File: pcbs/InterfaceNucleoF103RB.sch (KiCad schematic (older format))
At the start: 4 parts

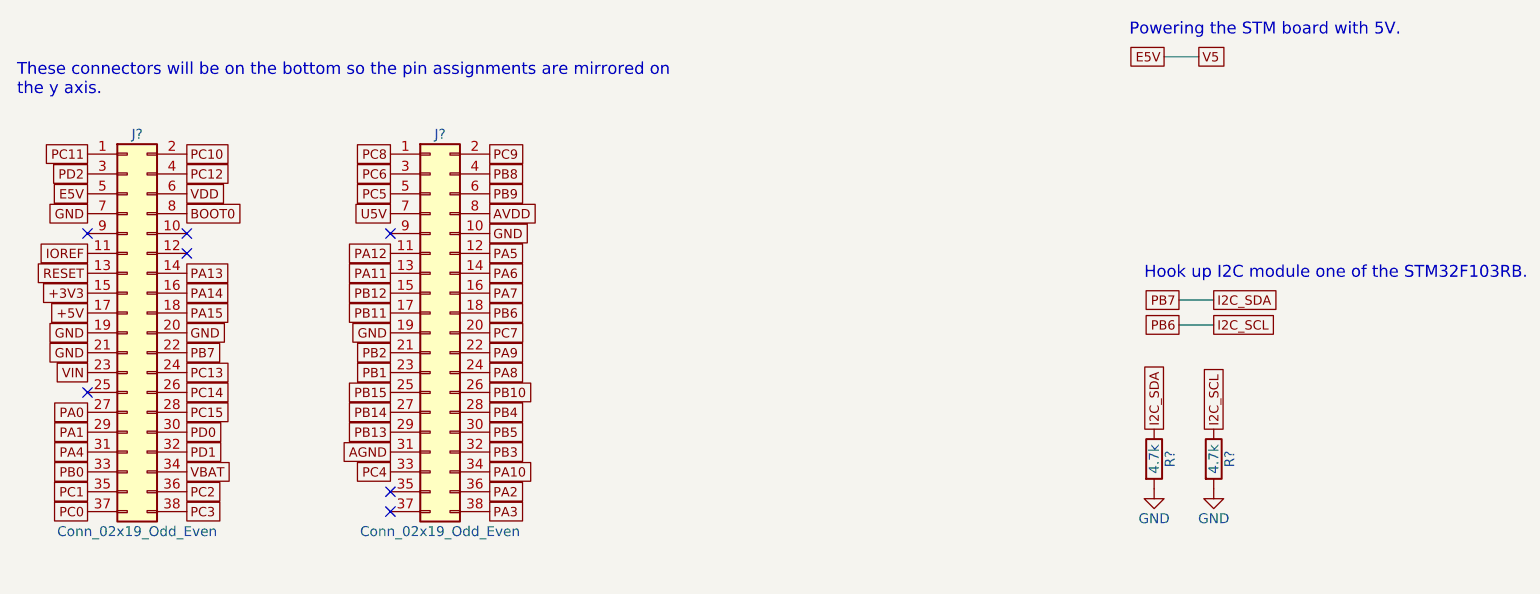
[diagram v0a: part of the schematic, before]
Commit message: Almost done with schematics. SPI OLED is missing.
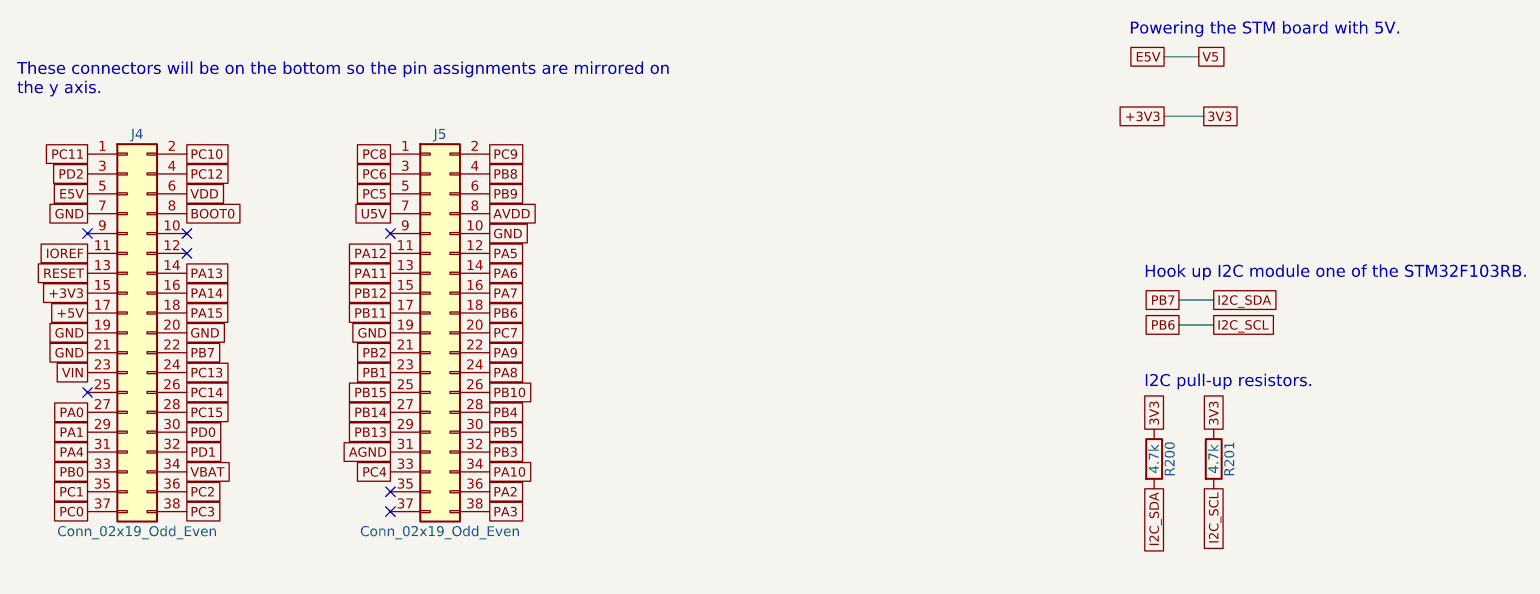
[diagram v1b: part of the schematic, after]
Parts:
- gave numbers to parts that had none: 4
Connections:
- net +3V3: now also R200.1, R201.1
- net GND: no longer R200.2, R201.2
- net I2C_SCL: now also R201.2; no longer R201.1
- net I2C_SDA: now also R200.2; no longer R200.1
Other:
- note added: "I2C pull-up resistors."
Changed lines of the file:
@@
 LIBS:mydacs
 LIBS:mydcdcs
+LIBS:switches
+LIBS:mytactilesw
 LIBS:led_driver-cache
 EELAYER 25 0
@@
 $EndDescr
 $Comp
-L Conn_02x19_Odd_Even J?
+L Conn_02x19_Odd_Even J4
 U 1 1 5A0C4E25
 P 2830 3565
-F 0 "J?" H 2880 4565 50  0000 C CNN
+F 0 "J4" H 2880 4565 50  0000 C CNN
 F 1 "Conn_02x19_Odd_Even" H 2880 2565 50  0000 C CNN
 F 2 "" H 2830 3565 50  0001 C CNN
@@
 NoConn ~ 2630 3865
 $Comp
-L Conn_02x19_Odd_Even J?
+L Conn_02x19_Odd_Even J5
 U 1 1 5A0C5DFF
 P 4355 3565
-F 0 "J?" H 4405 4565 50  0000 C CNN
+F 0 "J5" H 4405 4565 50  0000 C CNN
 F 1 "Conn_02x19_Odd_Even" H 4405 2565 50  0000 C CNN
 F 2 "" H 4355 3565 50  0001 C CNN
@@
 Text GLabel 8225 2175 2    47   UnSpc ~ 0
 V5
-Wire Wire Line
-	8050 2175 8225 2175
 Text Notes 7875 2075 0    60   ~ 0
 Powering the STM board with 5V.
@@
 Text GLabel 8300 3400 2    47   UnSpc ~ 0
 I2C_SDA
-Wire Wire Line
-	8125 3400 8300 3400
 Text GLabel 8125 3525 0    47   UnSpc ~ 0
 PB6
 Text GLabel 8300 3525 2    47   UnSpc ~ 0
 I2C_SCL
-Wire Wire Line
-	8125 3525 8300 3525
-$Comp
-L R R?
+$Comp
+L R R200
 U 1 1 5A0C91BF
 P 8000 4200
-F 0 "R?" V 8080 4200 50  0000 C CNN
+F 0 "R200" V 8080 4200 50  0000 C CNN
 F 1 "4.7k" V 8000 4200 50  0000 C CNN
 F 2 "Resistors_SMD:R_0603" V 7930 4200 50  0001 C CNN
@@
 $EndComp
 $Comp
-L R R?
+L R R201
 U 1 1 5A0C92CA
 P 8300 4200
-F 0 "R?" V 8380 4200 50  0000 C CNN
+F 0 "R201" V 8380 4200 50  0000 C CNN
 F 1 "4.7k" V 8300 4200 50  0000 C CNN
 F 2 "Resistors_SMD:R_0603" V 8230 4200 50  0001 C CNN
@@
 	1    0    0    -1
 $EndComp
+Text GLabel 8300 4350 3    47   UnSpc ~ 0
+I2C_SCL
+Text GLabel 8000 4350 3    47   UnSpc ~ 0
+I2C_SDA
+Text GLabel 8050 2475 0    47   UnSpc ~ 0
++3V3
+Text GLabel 8250 2475 2    47   UnSpc ~ 0
+3V3
+Text GLabel 8000 4050 1    47   UnSpc ~ 0
+3V3
 Text GLabel 8300 4050 1    47   UnSpc ~ 0
-I2C_SCL
-Text GLabel 8000 4050 1    47   UnSpc ~ 0
-I2C_SDA
-$Comp
-L GND #PWR?
-U 1 1 5A0C94D9
-P 8000 4350
-F 0 "#PWR?" H 8000 4100 50  0001 C CNN
-F 1 "GND" H 8000 4200 50  0000 C CNN
-F 2 "" H 8000 4350 50  0001 C CNN
-F 3 "" H 8000 4350 50  0001 C CNN
-	1    8000 4350
-	1    0    0    -1
-$EndComp
-$Comp
-L GND #PWR?
-U 1 1 5A0C94F7
-P 8300 4350
-F 0 "#PWR?" H 8300 4100 50  0001 C CNN
-F 1 "GND" H 8300 4200 50  0000 C CNN
-F 2 "" H 8300 4350 50  0001 C CNN
-F 3 "" H 8300 4350 50  0001 C CNN
-	1    8300 4350
-	1    0    0    -1
-$EndComp
+3V3
+Wire Wire Line
+	8050 2175 8225 2175
+Wire Wire Line
+	8125 3400 8300 3400
+Wire Wire Line
+	8125 3525 8300 3525
+Wire Wire Line
+	8050 2475 8250 2475
+Text Notes 7950 3850 0    60   ~ 0
+I2C pull-up resistors.
 $EndSCHEMATC

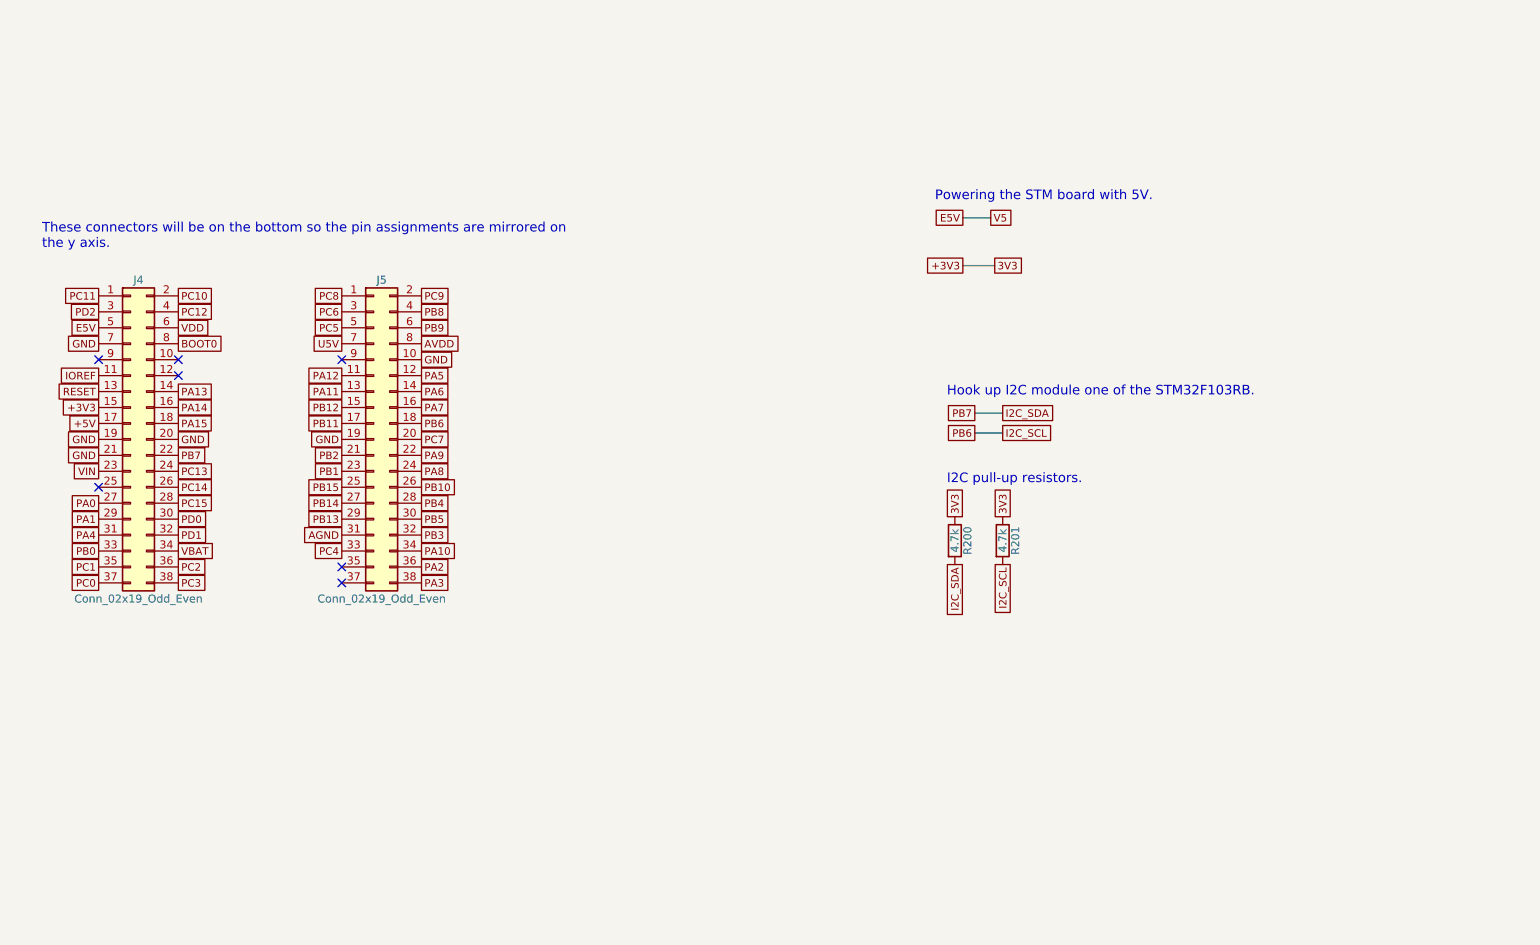
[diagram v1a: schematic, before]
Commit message: No DRC errors anymore in schematics.
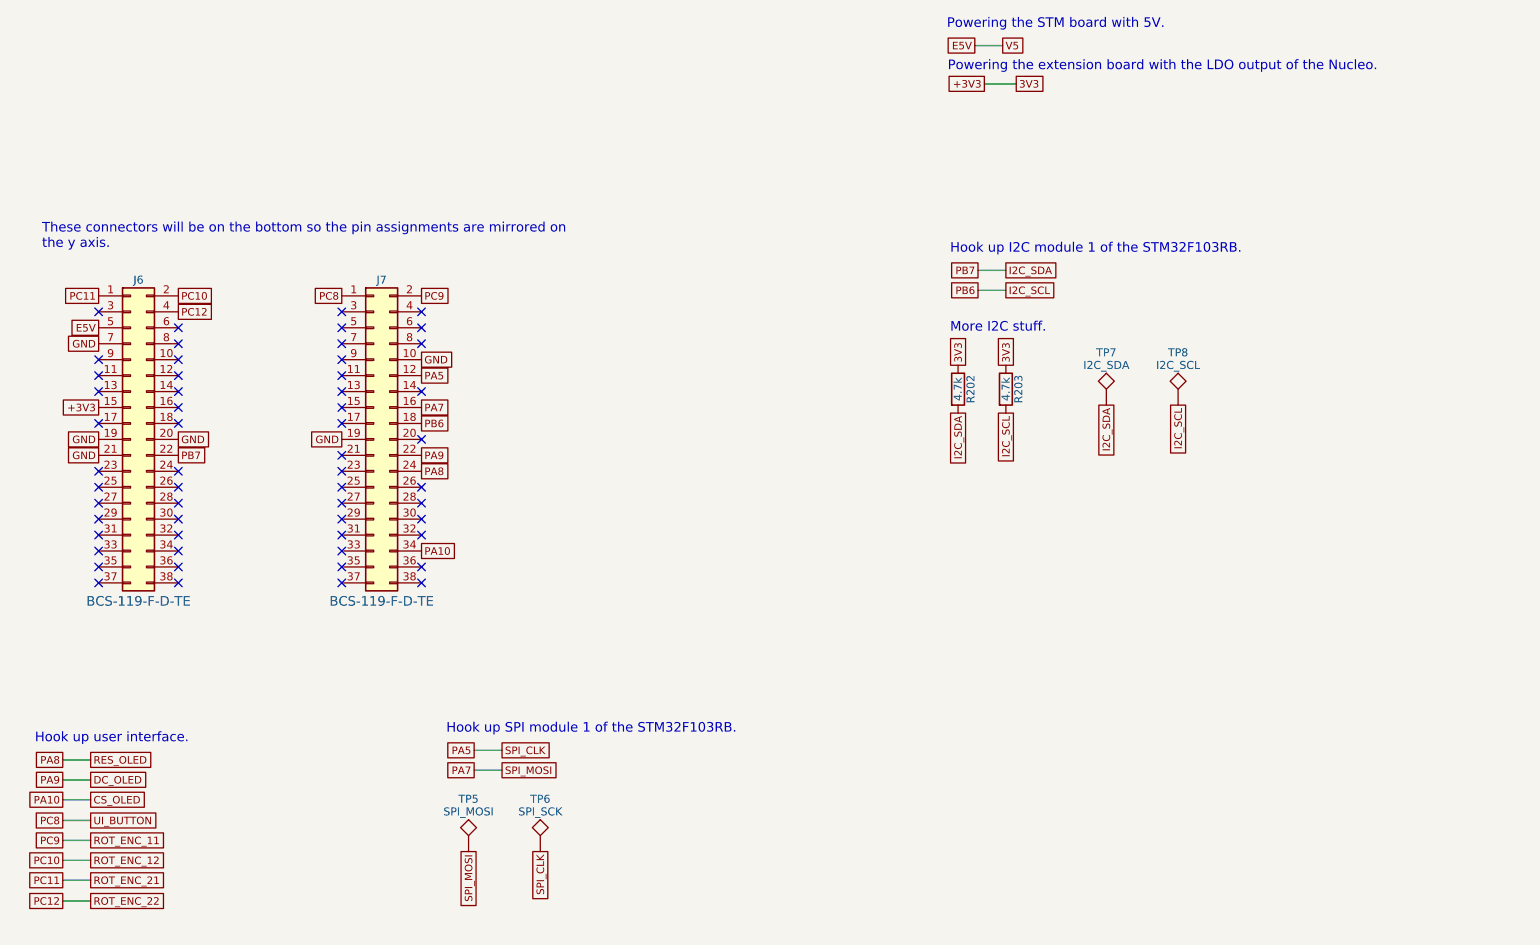
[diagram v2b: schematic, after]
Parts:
- removed J5: Conn_02x19_Odd_Even, symbol Conn_02x19_Odd_Even
- added J7: Conn_02x19_Odd_Even, Pin_Headers:Pin_Header_Straight_2x19_Pitch2.54mm, symbol Conn_02x19_Odd_Even
- added TP5: SPI_MOSI, MyTestpoints:TP_SMD_quadr_1mm, symbol TEST
- added TP6: SPI_SCK, MyTestpoints:TP_SMD_quadr_1mm, symbol TEST
- added TP7: I2C_SDA, MyTestpoints:TP_SMD_quadr_1mm, symbol TEST
- added TP8: I2C_SCL, MyTestpoints:TP_SMD_quadr_1mm, symbol TEST
- J6: renamed from J4; footprint (none) -> Pin_Headers:Pin_Header_Straight_2x19_Pitch2.54mm; Samtec (none) -> BCS-119-F-D-TE
- renumbered R200 to R202, R201 to R203
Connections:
- net GND: now also J7.10 (Pin_10), J7.19 (Pin_19)
- net I2C_SCL: now also J7.18 (Pin_18), TP8.1
- net I2C_SDA: now also TP7.1
- net PA5: now also J7.12 (Pin_12), TP6.1
- net PA7: now also J7.16 (Pin_16), TP5.1
- net PA8: now also J7.24 (Pin_24)
- net PC8: now also J7.1 (Pin_1)
- net PC9: now also J7.2 (Pin_2)
- net +5V: no longer names the net of J6.17 (Pin_17)
- net BOOT0: no longer names the net of J6.8 (Pin_8)
- net IOREF: no longer names the net of J6.11 (Pin_11)
- net PA0: no longer names the net of J6.27 (Pin_27)
- net PA1: no longer names the net of J6.29 (Pin_29)
- net PA13: no longer names the net of J6.14 (Pin_14)
- net PA14: no longer names the net of J6.16 (Pin_16)
- net PA15: no longer names the net of J6.18 (Pin_18)
- net PA4: no longer names the net of J6.31 (Pin_31)
- net PB0: no longer names the net of J6.33 (Pin_33)
- net PC0: no longer names the net of J6.37 (Pin_37)
- net PC1: no longer names the net of J6.35 (Pin_35)
- net PC13: no longer names the net of J6.24 (Pin_24)
- net PC14: no longer names the net of J6.26 (Pin_26)
- net PC15: no longer names the net of J6.28 (Pin_28)
- net PC2: no longer names the net of J6.36 (Pin_36)
- net PC3: no longer names the net of J6.38 (Pin_38)
- net PD0: no longer names the net of J6.30 (Pin_30)
- net PD1: no longer names the net of J6.32 (Pin_32)
- net PD2: no longer names the net of J6.3 (Pin_3)
- net RESET: no longer names the net of J6.13 (Pin_13)
- net VBAT: no longer names the net of J6.34 (Pin_34)
- net VDD: no longer names the net of J6.6 (Pin_6)
- net VIN: no longer names the net of J6.23 (Pin_23)
- new net CS_OLED: J7.34 (Pin_34)
- new net DC_OLED: J7.22 (Pin_22)
- no-connect marks 7 -> 56
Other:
- note added: "Hook up I2C module 1 of the STM32F103RB."
- note added: "Hook up SPI module 1 of the STM32F103RB."
- note added: "Hook up user interface."
- note added: "More I2C stuff."
- note added: "Powering the extension board with the LDO output of the Nucleo."
- note removed: "Hook up I2C module one of the STM32F103RB."
- note removed: "I2C pull-up resistors."
- moved on the sheet: R202, R203
